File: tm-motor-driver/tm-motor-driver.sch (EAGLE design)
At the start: 18 parts

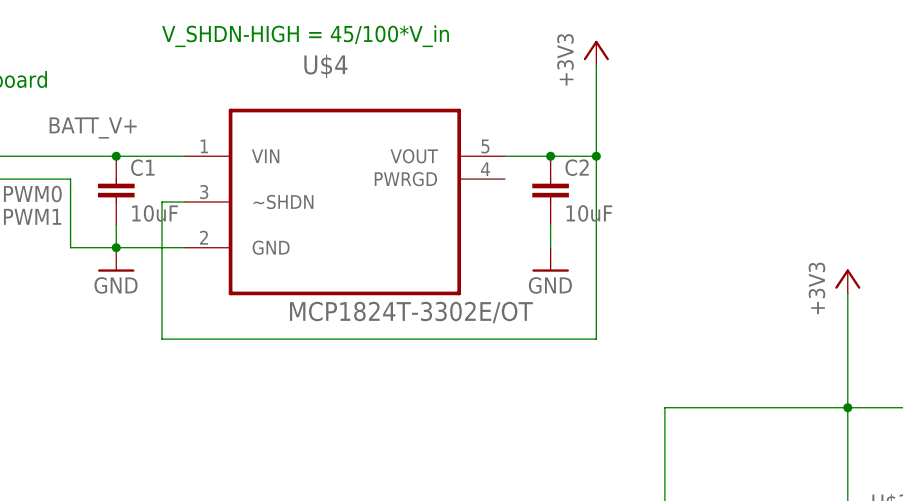
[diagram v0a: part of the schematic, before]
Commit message: Add R on power good
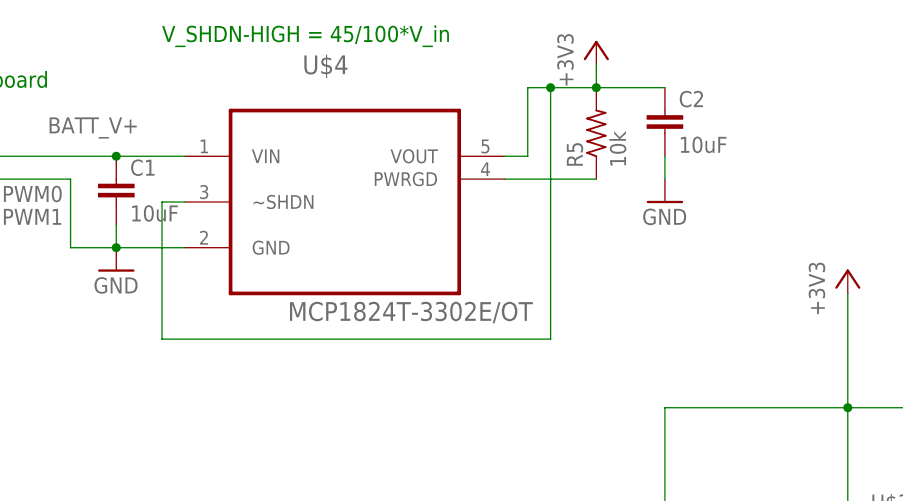
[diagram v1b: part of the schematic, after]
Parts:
- added R5: 10k, resistor:R-US_R0805
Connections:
- new net N$7: R5.1, U$4.PWRGD
- net +3V3: now also R5.2
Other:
- moved on the sheet: C2
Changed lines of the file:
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@@
 <part name="GND6" library="supply1" deviceset="GND" device=""/>
 <part name="C2" library="rcl" deviceset="C-EU" device="C0805" value="10uF"/>
+<part name="R5" library="resistor" deviceset="R-US_" device="R0805" value="10k"/>
 </parts>
 <sheets>
@@
 <instance part="C1" gate="G$1" x="38.1" y="149.86"/>
 <instance part="GND1" gate="1" x="38.1" y="139.7"/>
-<instance part="GND6" gate="1" x="86.36" y="139.7"/>
-<instance part="C2" gate="G$1" x="86.36" y="149.86"/>
+<instance part="GND6" gate="1" x="99.06" y="147.32"/>
+<instance part="C2" gate="G$1" x="99.06" y="157.48"/>
+<instance part="R5" gate="G$1" x="91.44" y="154.94" rot="R90"/>
 </instances>
 <busses>
@@
 </segment>
 <segment>
+<pinref part="C2" gate="G$1" pin="2"/>
 <pinref part="GND6" gate="1" pin="GND"/>
-<pinref part="C2" gate="G$1" pin="2"/>
-<wire x1="86.36" y1="142.24" x2="86.36" y2="144.78" width="0.1524" layer="91"/>
+<wire x1="99.06" y1="152.4" x2="99.06" y2="149.86" width="0.1524" layer="91"/>
 </segment>
 </net>
 <net name="+3V3" class="0">
-<segment>
-<pinref part="U$4" gate="A" pin="VOUT"/>
-<pinref part="+3V1" gate="G$1" pin="+3V3"/>
-<wire x1="81.28" y1="152.4" x2="86.36" y2="152.4" width="0.1524" layer="91"/>
-<wire x1="86.36" y1="152.4" x2="91.44" y2="152.4" width="0.1524" layer="91"/>
-<wire x1="91.44" y1="152.4" x2="91.44" y2="162.56" width="0.1524" layer="91"/>
-<pinref part="U$4" gate="A" pin="~SHDN"/>
-<wire x1="45.72" y1="147.32" x2="43.18" y2="147.32" width="0.1524" layer="91"/>
-<wire x1="43.18" y1="147.32" x2="43.18" y2="132.08" width="0.1524" layer="91"/>
-<wire x1="43.18" y1="132.08" x2="91.44" y2="132.08" width="0.1524" layer="91"/>
-<wire x1="91.44" y1="132.08" x2="91.44" y2="152.4" width="0.1524" layer="91"/>
-<junction x="91.44" y="152.4"/>
-<pinref part="C2" gate="G$1" pin="1"/>
-<junction x="86.36" y="152.4"/>
-</segment>
 <segment>
 <pinref part="JP2" gate="A" pin="1"/>
@@
 <pinref part="U$7" gate="G$1" pin="1"/>
 <wire x1="200.66" y1="109.22" x2="200.66" y2="124.46" width="0.1524" layer="91"/>
+</segment>
+<segment>
+<pinref part="R5" gate="G$1" pin="2"/>
+<pinref part="+3V1" gate="G$1" pin="+3V3"/>
+<wire x1="91.44" y1="160.02" x2="91.44" y2="162.56" width="0.1524" layer="91"/>
+<pinref part="U$4" gate="A" pin="VOUT"/>
+<wire x1="81.28" y1="152.4" x2="83.82" y2="152.4" width="0.1524" layer="91"/>
+<wire x1="83.82" y1="152.4" x2="83.82" y2="160.02" width="0.1524" layer="91"/>
+<wire x1="83.82" y1="160.02" x2="86.36" y2="160.02" width="0.1524" layer="91"/>
+<junction x="91.44" y="160.02"/>
+<pinref part="C2" gate="G$1" pin="1"/>
+<wire x1="86.36" y1="160.02" x2="91.44" y2="160.02" width="0.1524" layer="91"/>
+<wire x1="99.06" y1="160.02" x2="91.44" y2="160.02" width="0.1524" layer="91"/>
+<pinref part="U$4" gate="A" pin="~SHDN"/>
+<wire x1="45.72" y1="147.32" x2="43.18" y2="147.32" width="0.1524" layer="91"/>
+<wire x1="43.18" y1="147.32" x2="43.18" y2="132.08" width="0.1524" layer="91"/>
+<wire x1="43.18" y1="132.08" x2="86.36" y2="132.08" width="0.1524" layer="91"/>
+<wire x1="86.36" y1="132.08" x2="86.36" y2="160.02" width="0.1524" layer="91"/>
+<junction x="86.36" y="160.02"/>
 </segment>
 </net>
@@
 </segment>
 </net>
+<net name="N$7" class="0">
+<segment>
+<pinref part="U$4" gate="A" pin="PWRGD"/>
+<pinref part="R5" gate="G$1" pin="1"/>
+<wire x1="81.28" y1="149.86" x2="91.44" y2="149.86" width="0.1524" layer="91"/>
+</segment>
+</net>

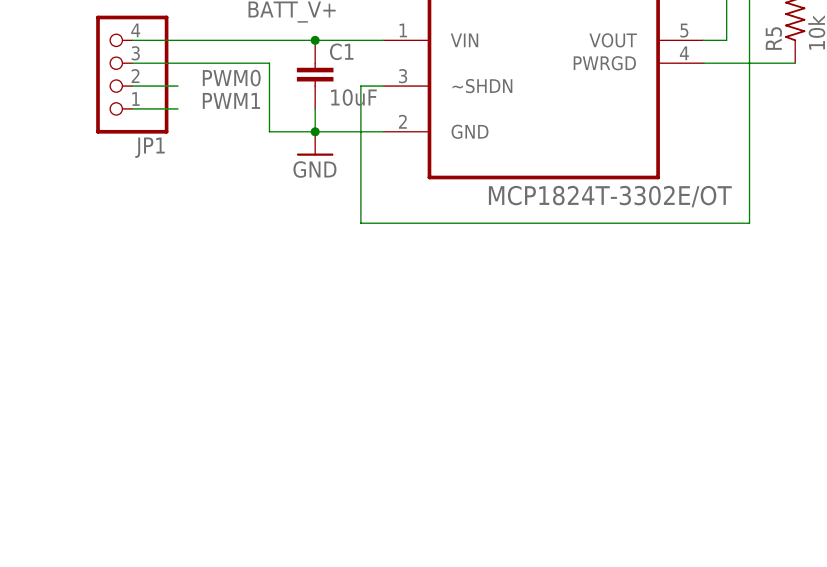
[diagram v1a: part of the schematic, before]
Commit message: Add note about input cap size choice
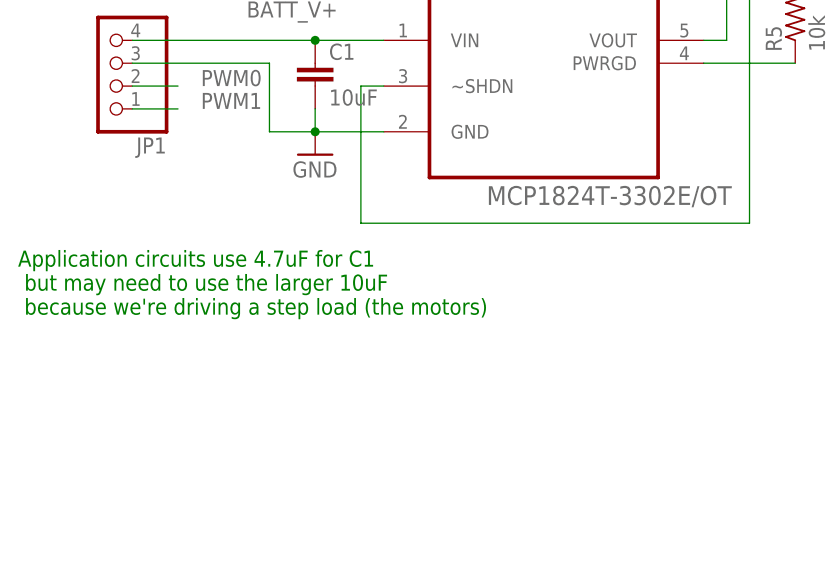
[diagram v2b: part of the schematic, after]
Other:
- note added: "Application circuits use 4.7uF for C1 but may need to use the larger 10uF because we're driving a step load (the motors)"
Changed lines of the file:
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@@
 <text x="129.54" y="106.68" size="1.778" layer="91">To motor</text>
 <text x="210.82" y="106.68" size="1.778" layer="91">To motor</text>
+<text x="5.08" y="121.92" size="1.778" layer="91">Application circuits use 4.7uF for C1
+ but may need to use the larger 10uF
+ because we're driving a step load (the motors)</text>
 </plain>
 <instances>
@@
 </schematic>
 </drawing>
+<compatibility>
+<note version="6.3" minversion="6.2.2" severity="warning">
+Since Version 6.2.2 text objects can contain more than one line,
+which will not be processed correctly with this version.
+</note>
+</compatibility>
 </eagle>

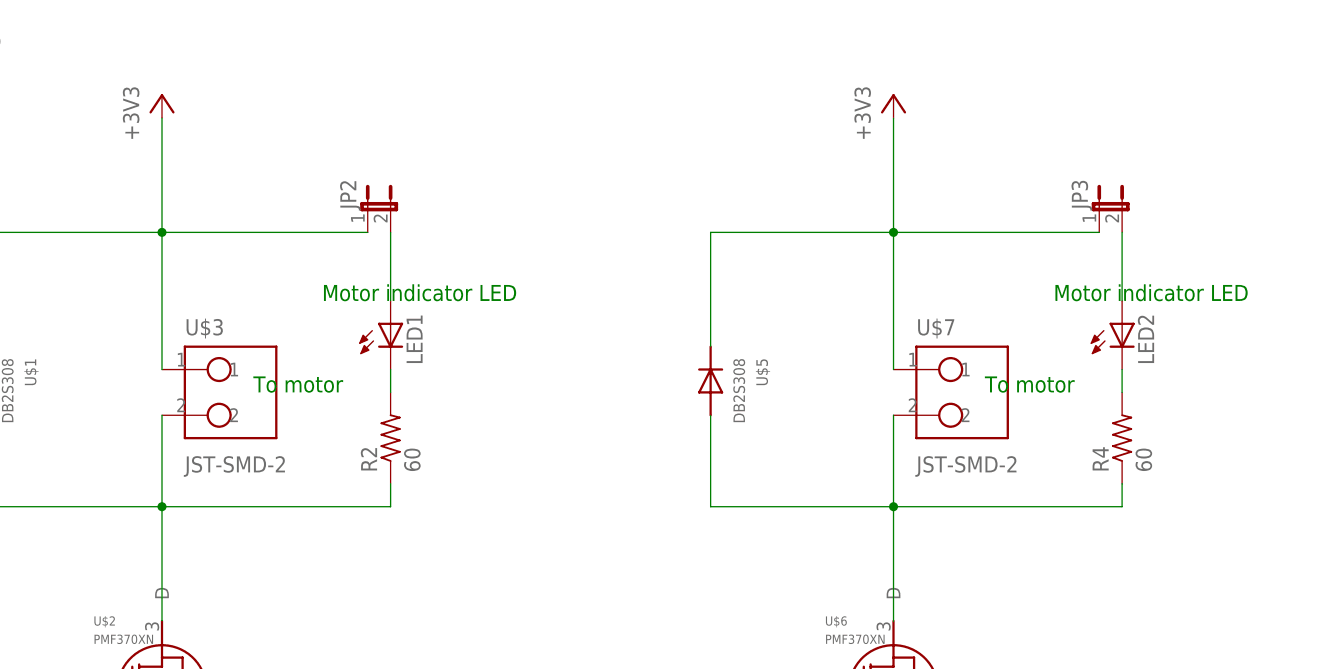
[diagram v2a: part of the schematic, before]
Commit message: Remove jumpers, rearrange LED and series resistor for easier layout
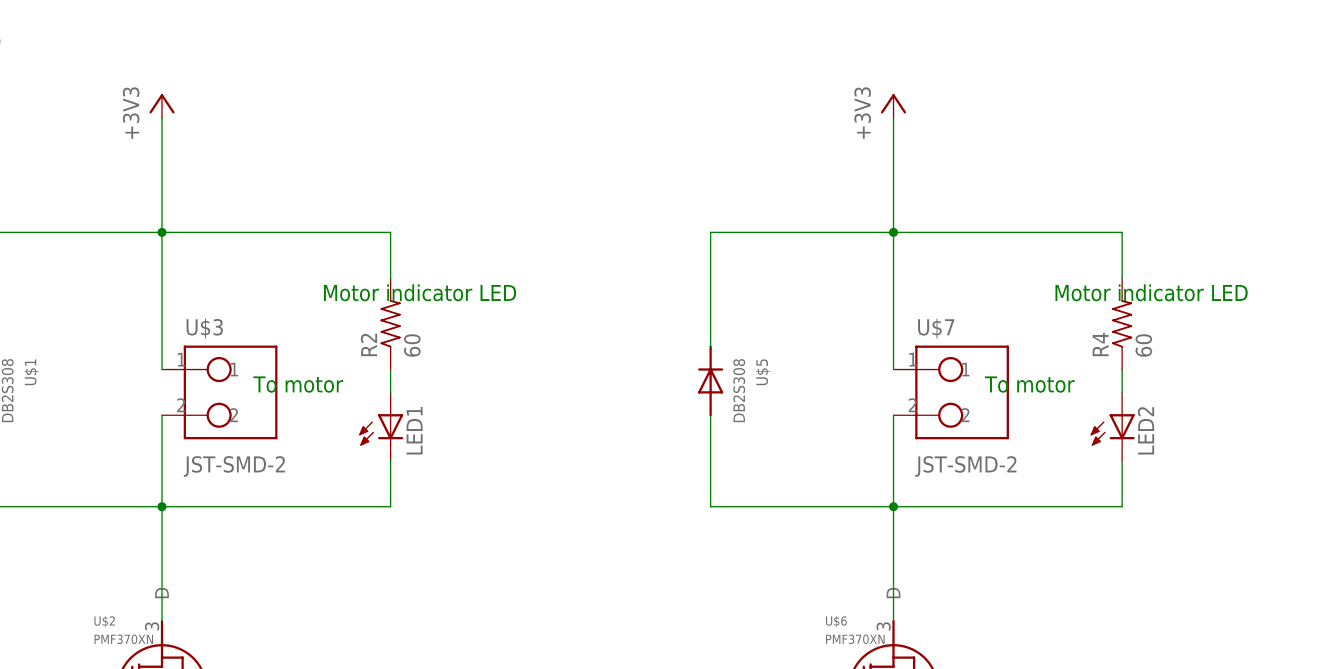
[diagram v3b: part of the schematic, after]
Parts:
- removed JP2, JP3: (no value), jumper:JP1E
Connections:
- removed net N$5: JP3.2, LED2.A
- removed net N$6: LED2.C, R4.2
- net +3V3: now also R2.2, R4.2; no longer JP2.1, JP3.1
- net N$1: now also LED2.C; no longer R4.1
- net N$2: now also LED1.C; no longer R2.1
- net N$3: now also R2.1; no longer JP2.2
- net N$4: now also LED2.A, R4.1; no longer LED1.C, R2.2
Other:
- moved on the sheet: LED1, LED2, R2, R4
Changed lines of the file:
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@@
 <part name="JP1" library="pinhead" deviceset="PINHD-1X4" device=""/>
 <part name="R2" library="resistor" deviceset="R-US_" device="R0805" value="60"/>
-<part name="JP2" library="jumper" deviceset="JP1E" device=""/>
 <part name="GND2" library="supply1" deviceset="GND" device=""/>
 <part name="GND3" library="supply1" deviceset="GND" device=""/>
@@
 <part name="LED2" library="led" deviceset="LED" device="CHIPLED_0805"/>
 <part name="R4" library="resistor" deviceset="R-US_" device="R0805" value="60"/>
-<part name="JP3" library="jumper" deviceset="JP1E" device=""/>
 <part name="GND4" library="supply1" deviceset="GND" device=""/>
 <part name="GND5" library="supply1" deviceset="GND" device=""/>
@@
 <instance part="U$3" gate="G$1" x="127" y="106.68"/>
 <instance part="R1" gate="G$1" x="99.06" y="63.5" rot="R90"/>
-<instance part="LED1" gate="G$1" x="144.78" y="114.3"/>
+<instance part="LED1" gate="G$1" x="144.78" y="104.14"/>
 <instance part="U$4" gate="A" x="63.5" y="149.86"/>
 <instance part="JP1" gate="A" x="15.24" y="149.86" rot="R180"/>
-<instance part="R2" gate="G$1" x="144.78" y="101.6" rot="R90"/>
-<instance part="JP2" gate="A" x="142.24" y="127"/>
+<instance part="R2" gate="G$1" x="144.78" y="114.3" rot="R90"/>
 <instance part="GND2" gate="1" x="99.06" y="53.34"/>
 <instance part="GND3" gate="1" x="119.38" y="53.34"/>
@@
 <instance part="U$7" gate="G$1" x="208.28" y="106.68"/>
 <instance part="R3" gate="G$1" x="180.34" y="63.5" rot="R90"/>
-<instance part="LED2" gate="G$1" x="226.06" y="114.3"/>
-<instance part="R4" gate="G$1" x="226.06" y="101.6" rot="R90"/>
-<instance part="JP3" gate="A" x="223.52" y="127"/>
+<instance part="LED2" gate="G$1" x="226.06" y="104.14"/>
+<instance part="R4" gate="G$1" x="226.06" y="114.3" rot="R90"/>
 <instance part="GND4" gate="1" x="180.34" y="53.34"/>
 <instance part="GND5" gate="1" x="200.66" y="53.34"/>
@@
 <net name="+3V3" class="0">
 <segment>
-<pinref part="JP2" gate="A" pin="1"/>
 <pinref part="+3V2" gate="G$1" pin="+3V3"/>
-<wire x1="142.24" y1="124.46" x2="119.38" y2="124.46" width="0.1524" layer="91"/>
 <wire x1="119.38" y1="124.46" x2="119.38" y2="137.16" width="0.1524" layer="91"/>
 <pinref part="U$1" gate="G$1" pin="CATHODE"/>
@@
 <pinref part="U$3" gate="G$1" pin="1"/>
 <wire x1="119.38" y1="109.22" x2="119.38" y2="124.46" width="0.1524" layer="91"/>
-</segment>
-<segment>
-<pinref part="JP3" gate="A" pin="1"/>
+<wire x1="119.38" y1="124.46" x2="144.78" y2="124.46" width="0.1524" layer="91"/>
+<pinref part="R2" gate="G$1" pin="2"/>
+<wire x1="144.78" y1="119.38" x2="144.78" y2="124.46" width="0.1524" layer="91"/>
+</segment>
+<segment>
 <pinref part="+3V3" gate="G$1" pin="+3V3"/>
-<wire x1="223.52" y1="124.46" x2="200.66" y2="124.46" width="0.1524" layer="91"/>
 <wire x1="200.66" y1="124.46" x2="200.66" y2="137.16" width="0.1524" layer="91"/>
 <pinref part="U$5" gate="G$1" pin="CATHODE"/>
@@
 <pinref part="U$7" gate="G$1" pin="1"/>
 <wire x1="200.66" y1="109.22" x2="200.66" y2="124.46" width="0.1524" layer="91"/>
+<wire x1="200.66" y1="124.46" x2="226.06" y2="124.46" width="0.1524" layer="91"/>
+<pinref part="R4" gate="G$1" pin="2"/>
+<wire x1="226.06" y1="124.46" x2="226.06" y2="119.38" width="0.1524" layer="91"/>
 </segment>
 <segment>
@@
 <pinref part="U$3" gate="G$1" pin="2"/>
 <wire x1="119.38" y1="81.28" x2="119.38" y2="93.98" width="0.1524" layer="91"/>
-<pinref part="R2" gate="G$1" pin="1"/>
 <wire x1="119.38" y1="93.98" x2="119.38" y2="104.14" width="0.1524" layer="91"/>
 <wire x1="119.38" y1="93.98" x2="144.78" y2="93.98" width="0.1524" layer="91"/>
-<wire x1="144.78" y1="93.98" x2="144.78" y2="96.52" width="0.1524" layer="91"/>
 <junction x="119.38" y="93.98"/>
 <pinref part="U$1" gate="G$1" pin="ANODE"/>
 <wire x1="119.38" y1="93.98" x2="99.06" y2="93.98" width="0.1524" layer="91"/>
 <wire x1="99.06" y1="93.98" x2="99.06" y2="104.14" width="0.1524" layer="91"/>
-</segment>
-</net>
-<net name="N$3" class="0">
-<segment>
-<pinref part="JP2" gate="A" pin="2"/>
-<pinref part="LED1" gate="G$1" pin="A"/>
-<wire x1="144.78" y1="124.46" x2="144.78" y2="116.84" width="0.1524" layer="91"/>
-</segment>
-</net>
-<net name="N$4" class="0">
-<segment>
 <pinref part="LED1" gate="G$1" pin="C"/>
-<pinref part="R2" gate="G$1" pin="2"/>
-<wire x1="144.78" y1="109.22" x2="144.78" y2="106.68" width="0.1524" layer="91"/>
+<wire x1="144.78" y1="93.98" x2="144.78" y2="99.06" width="0.1524" layer="91"/>
 </segment>
 </net>
@@
 <pinref part="U$7" gate="G$1" pin="2"/>
 <wire x1="200.66" y1="81.28" x2="200.66" y2="93.98" width="0.1524" layer="91"/>
-<pinref part="R4" gate="G$1" pin="1"/>
 <wire x1="200.66" y1="93.98" x2="200.66" y2="104.14" width="0.1524" layer="91"/>
 <wire x1="200.66" y1="93.98" x2="226.06" y2="93.98" width="0.1524" layer="91"/>
-<wire x1="226.06" y1="93.98" x2="226.06" y2="96.52" width="0.1524" layer="91"/>
 <junction x="200.66" y="93.98"/>
 <pinref part="U$5" gate="G$1" pin="ANODE"/>
 <wire x1="200.66" y1="93.98" x2="180.34" y2="93.98" width="0.1524" layer="91"/>
 <wire x1="180.34" y1="93.98" x2="180.34" y2="104.14" width="0.1524" layer="91"/>
-</segment>
-</net>
-<net name="N$5" class="0">
-<segment>
-<pinref part="JP3" gate="A" pin="2"/>
-<pinref part="LED2" gate="G$1" pin="A"/>
-<wire x1="226.06" y1="124.46" x2="226.06" y2="116.84" width="0.1524" layer="91"/>
-</segment>
-</net>
-<net name="N$6" class="0">
-<segment>
 <pinref part="LED2" gate="G$1" pin="C"/>
-<pinref part="R4" gate="G$1" pin="2"/>
-<wire x1="226.06" y1="109.22" x2="226.06" y2="106.68" width="0.1524" layer="91"/>
+<wire x1="226.06" y1="99.06" x2="226.06" y2="93.98" width="0.1524" layer="91"/>
 </segment>
 </net>
@@
 </segment>
 </net>
+<net name="N$3" class="0">
+<segment>
+<pinref part="LED1" gate="G$1" pin="A"/>
+<pinref part="R2" gate="G$1" pin="1"/>
+<wire x1="144.78" y1="106.68" x2="144.78" y2="109.22" width="0.1524" layer="91"/>
+</segment>
+</net>
+<net name="N$4" class="0">
+<segment>
+<pinref part="R4" gate="G$1" pin="1"/>
+<pinref part="LED2" gate="G$1" pin="A"/>
+<wire x1="226.06" y1="109.22" x2="226.06" y2="106.68" width="0.1524" layer="91"/>
+</segment>
+</net>
